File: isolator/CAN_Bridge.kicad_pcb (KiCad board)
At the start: 2 copper layers, 64 x 57.6 mm, 45 parts, among them J1 BOOT1, J2 BOOT0, J4 JTAG5, J5 USART1, J7 HIGHVOLTAGE CAN, J8 LOWVOLTAGE CAN, SW2 SW_Push, U1 STM32F105RBTx, U2 ISO1050DUB, U4 AZ1117CH-3.3TRG1, U5 MAX3051ESA+, U6 RSH3-1205S, Y2 406C35E25M00000

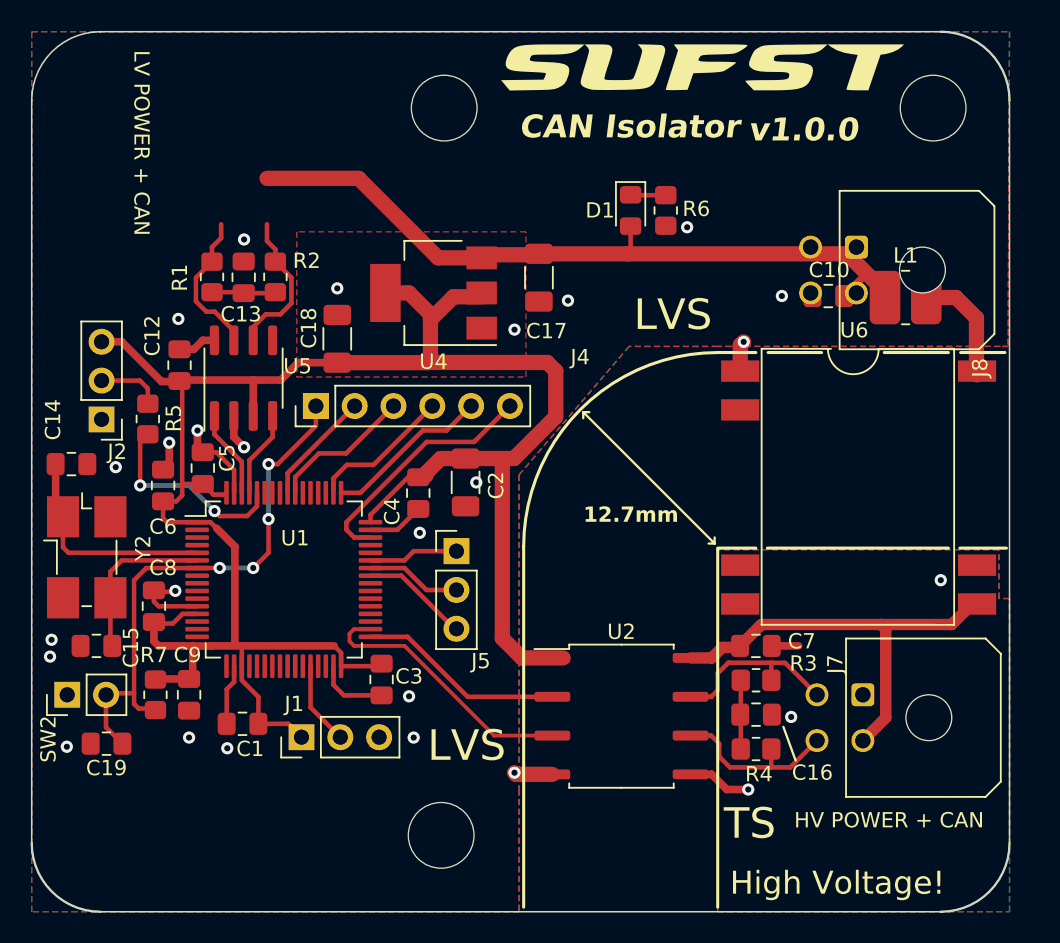
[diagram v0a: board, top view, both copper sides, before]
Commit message: Revert proposed PCB changes
STEP has components in wrong locations
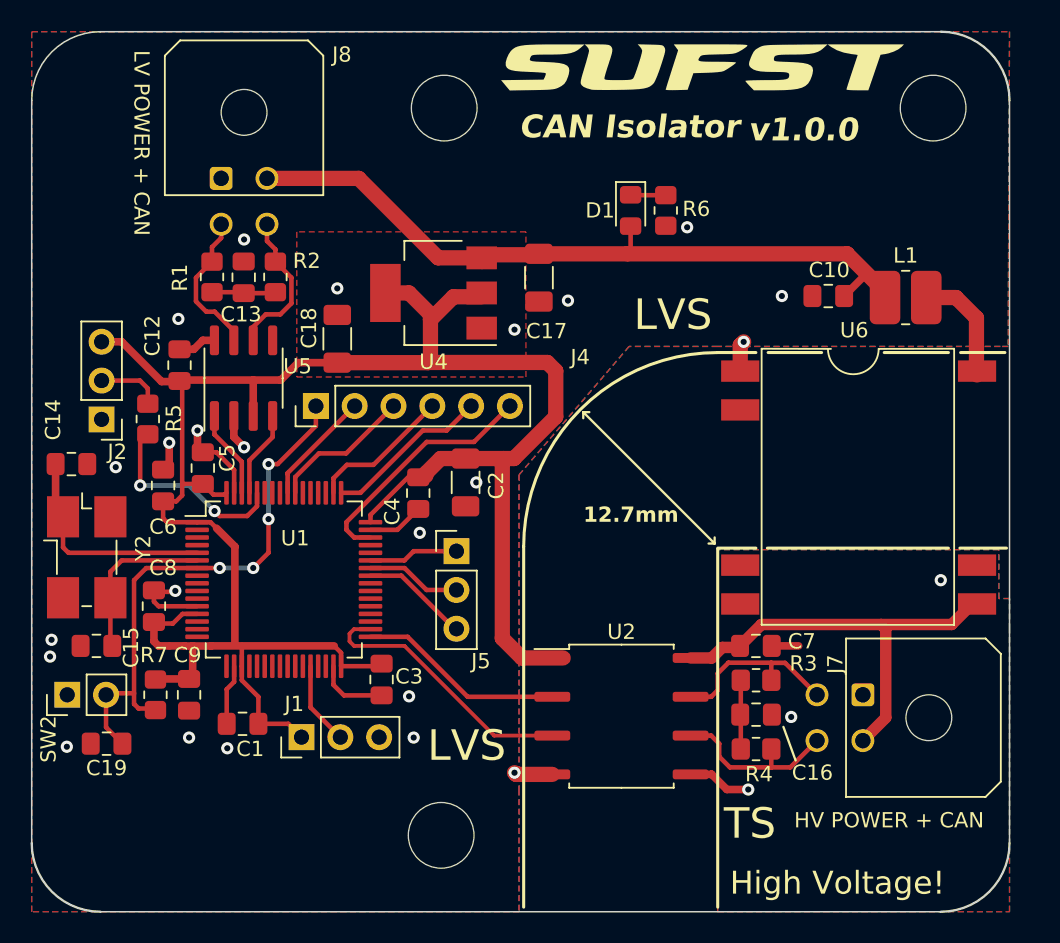
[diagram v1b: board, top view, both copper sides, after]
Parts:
- moved J8 41.8 mm to (143.3, 66.5), turned to 0 degrees
